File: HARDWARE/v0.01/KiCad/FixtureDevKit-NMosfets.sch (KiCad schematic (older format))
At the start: 32 parts, among them J71 NFET_0, J72 NFET_4, J73 NFET_1, J74 NFET_5, J75 NFET_2, J76 NFET_6, J77 NFET_3, J78 NFET_7, Q13 FDN337N, Q14 FDN337N, Q15 FDN337N, Q16 FDN337N, Q17 FDN337N, Q18 FDN337N, Q19 FDN337N, Q20 FDN337N

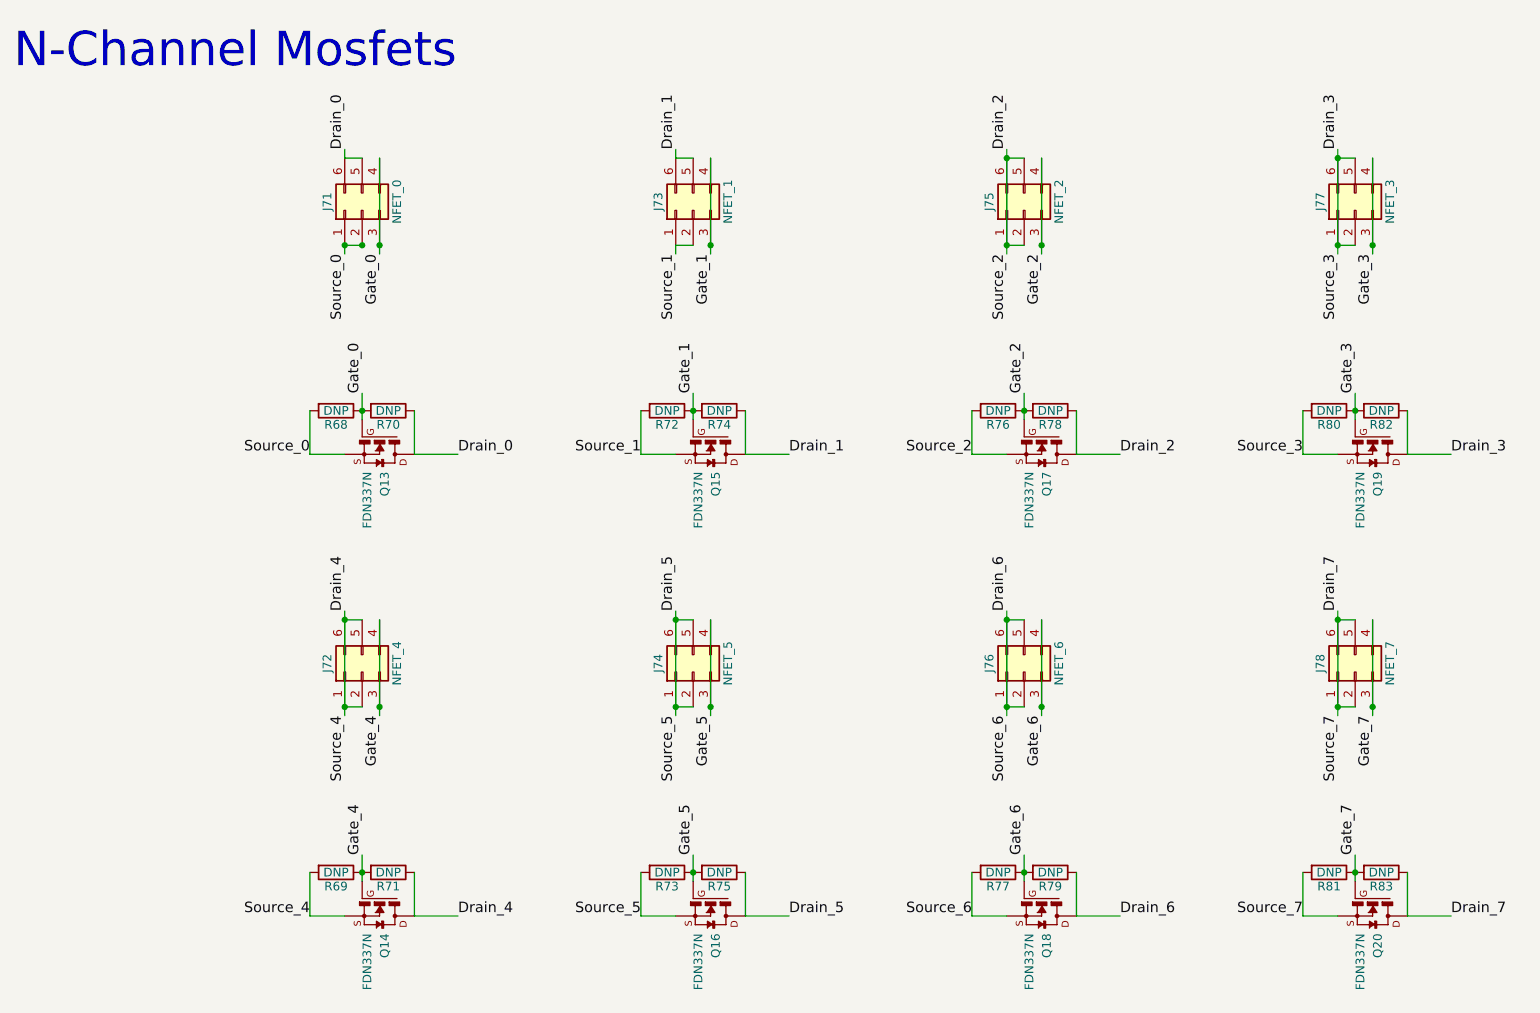
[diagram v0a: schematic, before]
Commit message: quasi-redoing entire schematic and layout
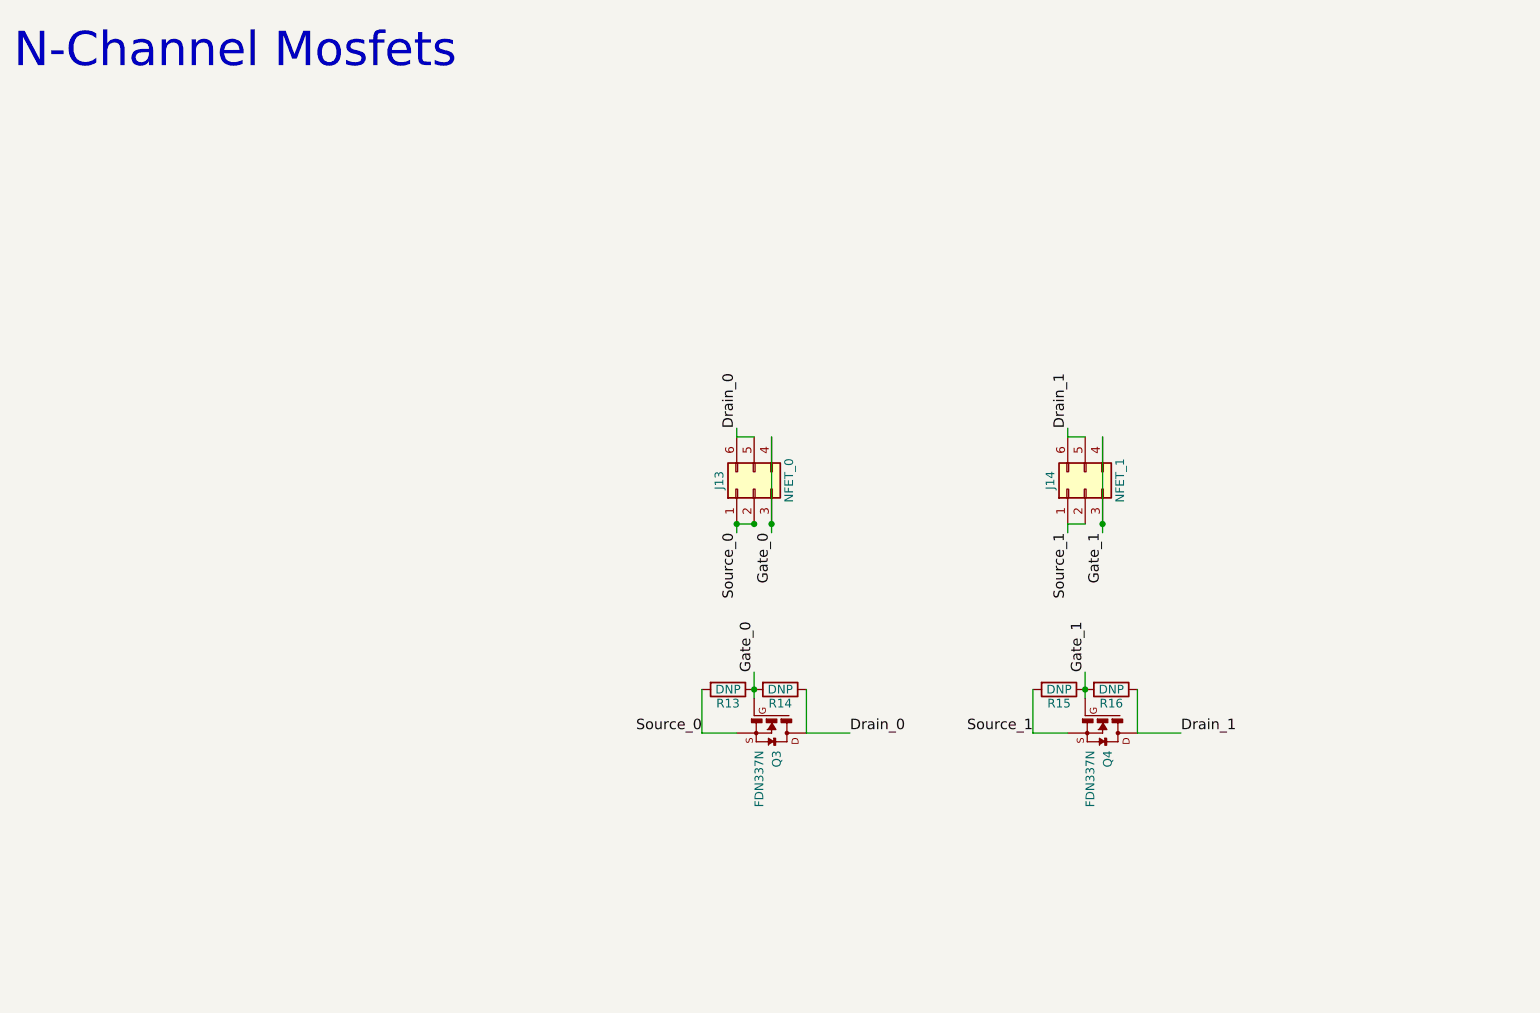
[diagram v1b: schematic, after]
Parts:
- removed J72: NFET_4, Pin_Headers:Pin_Header_Straight_2x03_Pitch2.54mm, symbol Conn_02x03_Counter_Clockwise
- removed J74: NFET_5, Pin_Headers:Pin_Header_Straight_2x03_Pitch2.54mm, symbol Conn_02x03_Counter_Clockwise
- removed J75: NFET_2, Pin_Headers:Pin_Header_Straight_2x03_Pitch2.54mm, symbol Conn_02x03_Counter_Clockwise
- removed J76: NFET_6, Pin_Headers:Pin_Header_Straight_2x03_Pitch2.54mm, symbol Conn_02x03_Counter_Clockwise
- removed J77: NFET_3, Pin_Headers:Pin_Header_Straight_2x03_Pitch2.54mm, symbol Conn_02x03_Counter_Clockwise
- removed J78: NFET_7, Pin_Headers:Pin_Header_Straight_2x03_Pitch2.54mm, symbol Conn_02x03_Counter_Clockwise
- removed Q14, Q16, Q17, Q18, Q19, Q20: FDN337N, FDN337N:SSOT-3, symbol FDN337N
- removed R69, R71, R73, R75, R76, R77, R78, R79, R80, R81, R82, R83: DNP, Resistors_SMD:R_0805_HandSoldering, symbol R
- renumbered J71 to J13, J73 to J14, Q13 to Q3, Q15 to Q4, R68 to R13, R70 to R14, R72 to R15, R74 to R16
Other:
- moved on the sheet: J13, J14, Q3, Q4, R13, R14, R15, R16
